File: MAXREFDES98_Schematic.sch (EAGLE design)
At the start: 34 parts, among them U1 MB110S-TP, U2 MB110S-TP, U3 MAX5969AETB+

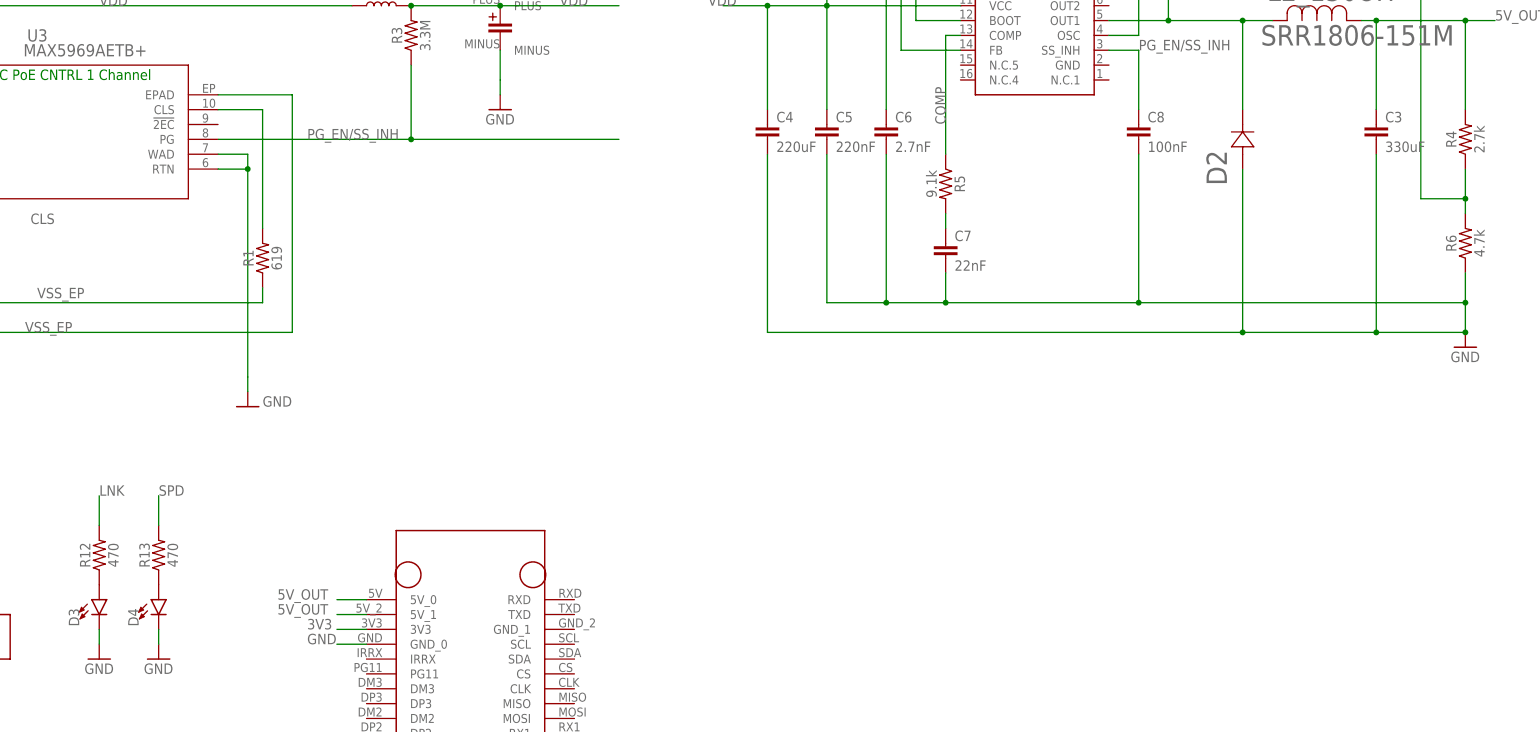
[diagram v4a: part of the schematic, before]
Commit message: Added new caps and leds
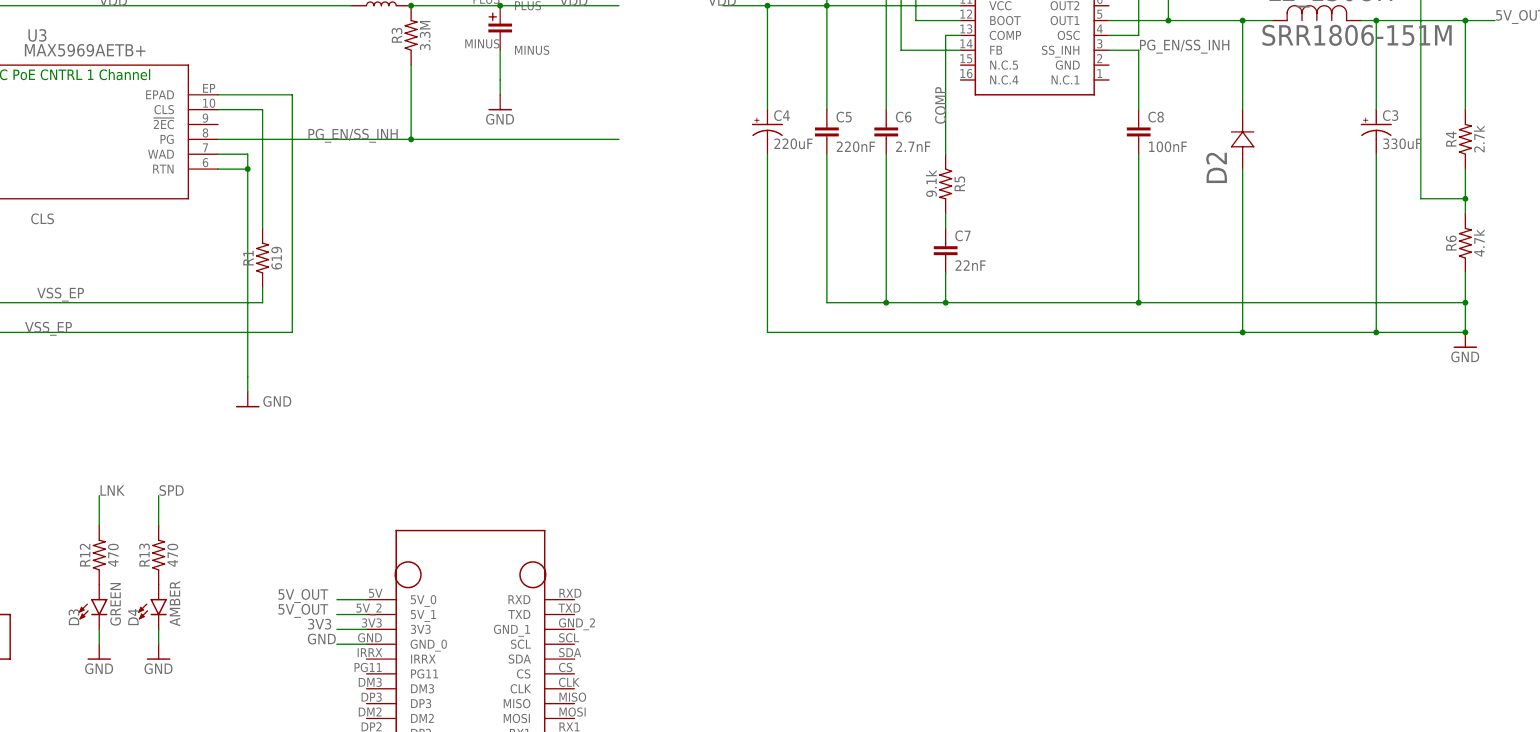
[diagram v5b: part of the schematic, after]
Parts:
- C3: value 330uF -> 337AXZ025M; device SparkFun-Capacitors:4.7UF0603 -> CameraBoard_Library:337AXZ025M
- C4: value 220uF -> EXV227M016A9HAA; device SparkFun-Capacitors:4.7UF0603 -> CameraBoard_Library:EXV227M016A9HAA
- D3: value (none) -> GREEN
- D4: value (none) -> AMBER
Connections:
- net 5V_OUT: now also C3.+; no longer C3.1
- net GND: now also C3.-, C4.-; no longer C3.2, C4.2
- net VDD: now also C4.+; no longer C4.1
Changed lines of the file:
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@@
 <part name="GND14" library="supply1" library_urn="urn:adsk.eagle:library:371" deviceset="GND" device=""/>
 <part name="U$1" library="Camera_Board_Parts_09_30_2020" deviceset="L4978D013TR" device="" package3d_urn="urn:adsk.eagle:package:24353853/1"/>
-<part name="C3" library="SparkFun-Capacitors" library_urn="urn:adsk.eagle:library:510" deviceset="4.7UF" device="0603" package3d_urn="urn:adsk.eagle:package:37414/1" value="330uF"/>
-<part name="C4" library="SparkFun-Capacitors" library_urn="urn:adsk.eagle:library:510" deviceset="4.7UF" device="0603" package3d_urn="urn:adsk.eagle:package:37414/1" value="220uF"/>
 <part name="C5" library="SparkFun-Capacitors" library_urn="urn:adsk.eagle:library:510" deviceset="4.7UF" device="0603" package3d_urn="urn:adsk.eagle:package:37414/1" value="220nF"/>
 <part name="C6" library="SparkFun-Capacitors" library_urn="urn:adsk.eagle:library:510" deviceset="4.7UF" device="0603" package3d_urn="urn:adsk.eagle:package:37414/1" value="2.7nF"/>
@@
 <part name="D2" library="Camera_Board_Parts_09_30_2020" deviceset="STPS3L60U" device="SMB_STM-M"/>
 <part name="GND2" library="supply1" library_urn="urn:adsk.eagle:library:371" deviceset="GND" device=""/>
-<part name="D3" library="SparkFun-LED" library_urn="urn:adsk.eagle:library:529" deviceset="LED" device="-FKIT-1206" package3d_urn="urn:adsk.eagle:package:39355/1"/>
-<part name="D4" library="SparkFun-LED" library_urn="urn:adsk.eagle:library:529" deviceset="LED" device="-FKIT-1206" package3d_urn="urn:adsk.eagle:package:39355/1"/>
+<part name="D3" library="SparkFun-LED" library_urn="urn:adsk.eagle:library:529" deviceset="LED" device="-FKIT-1206" package3d_urn="urn:adsk.eagle:package:39355/1" value="GREEN"/>
+<part name="D4" library="SparkFun-LED" library_urn="urn:adsk.eagle:library:529" deviceset="LED" device="-FKIT-1206" package3d_urn="urn:adsk.eagle:package:39355/1" value="AMBER"/>
 <part name="GND3" library="supply1" library_urn="urn:adsk.eagle:library:371" deviceset="GND" device=""/>
 <part name="GND4" library="supply1" library_urn="urn:adsk.eagle:library:371" deviceset="GND" device=""/>
@@
 <part name="L2_150UH" library="CameraBoard_Library" deviceset="SRR1806-151M" device=""/>
 <part name="U$2" library="CameraBoard_Library" deviceset="NANO_PI_CLEAN" device=""/>
+<part name="C4" library="CameraBoard_Library" deviceset="EXV227M016A9HAA" device=""/>
+<part name="C3" library="CameraBoard_Library" deviceset="337AXZ025M" device=""/>
 </parts>
 <sheets>
@@
 </instance>
 <instance part="U$1" gate="G$1" x="170.18" y="20.32" smashed="yes" rot="R180"/>
-<instance part="C3" gate="G$1" x="228.6" y="0" smashed="yes">
-<attribute name="NAME" x="230.124" y="2.921" size="1.778" layer="95" font="vector"/>
-<attribute name="VALUE" x="230.124" y="-2.159" size="1.778" layer="96" font="vector"/>
-</instance>
-<instance part="C4" gate="G$1" x="124.46" y="0" smashed="yes">
-<attribute name="NAME" x="125.984" y="2.921" size="1.778" layer="95" font="vector"/>
-<attribute name="VALUE" x="125.984" y="-2.159" size="1.778" layer="96" font="vector"/>
-</instance>
 <instance part="C5" gate="G$1" x="134.62" y="0" smashed="yes">
 <attribute name="NAME" x="136.144" y="2.921" size="1.778" layer="95" font="vector"/>
@@
 </instance>
 <instance part="U$2" gate="G$1" x="60.96" y="-121.92" smashed="yes"/>
+<instance part="C4" gate="G$1" x="124.46" y="2.54" smashed="yes">
+<attribute name="NAME" x="125.476" y="3.175" size="1.778" layer="95" font="vector"/>
+</instance>
+<instance part="C3" gate="G$1" x="228.6" y="2.54" smashed="yes">
+<attribute name="NAME" x="229.616" y="3.175" size="1.778" layer="95" font="vector"/>
+</instance>
 </instances>
 <busses>
@@
 <pinref part="U$1" gate="G$1" pin="VCC"/>
 <wire x1="157.48" y1="22.86" x2="134.62" y2="22.86" width="0.1524" layer="91"/>
-<pinref part="C4" gate="G$1" pin="1"/>
 <wire x1="134.62" y1="22.86" x2="124.46" y2="22.86" width="0.1524" layer="91"/>
 <wire x1="124.46" y1="22.86" x2="124.46" y2="5.08" width="0.1524" layer="91"/>
@@
 <junction x="124.46" y="22.86"/>
 <label x="114.3" y="22.86" size="1.778" layer="95"/>
+<pinref part="C4" gate="G$1" pin="+"/>
 </segment>
 <segment>
@@
 </segment>
 <segment>
-<pinref part="C3" gate="G$1" pin="1"/>
 <wire x1="228.6" y1="5.08" x2="228.6" y2="20.32" width="0.1524" layer="91"/>
 <wire x1="228.6" y1="20.32" x2="226.06" y2="20.32" width="0.1524" layer="91"/>
@@
 <label x="248.92" y="20.32" size="1.778" layer="95"/>
 <pinref part="L2_150UH" gate="A" pin="1"/>
+<pinref part="C3" gate="G$1" pin="+"/>
 </segment>
 <segment>
@@
 <wire x1="243.84" y1="-27.94" x2="243.84" y2="-33.02" width="0.1524" layer="91"/>
 <junction x="243.84" y="-27.94"/>
-<pinref part="C4" gate="G$1" pin="2"/>
 <wire x1="124.46" y1="-2.54" x2="124.46" y2="-33.02" width="0.1524" layer="91"/>
 <pinref part="D2" gate="A" pin="2"/>
@@
 <wire x1="205.74" y1="-33.02" x2="228.6" y2="-33.02" width="0.1524" layer="91"/>
 <junction x="205.74" y="-33.02"/>
-<pinref part="C3" gate="G$1" pin="2"/>
 <wire x1="228.6" y1="-33.02" x2="228.6" y2="-2.54" width="0.1524" layer="91"/>
 <wire x1="243.84" y1="-33.02" x2="228.6" y2="-33.02" width="0.1524" layer="91"/>
@@
 <pinref part="GND2" gate="1" pin="GND"/>
 <junction x="243.84" y="-33.02"/>
-</segment>
-<segment>
+<pinref part="C4" gate="G$1" pin="-"/>
+<pinref part="C3" gate="G$1" pin="-"/>
+</segment>
+<segment>

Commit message: Placement
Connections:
- new net VDD_L: C2.PLUS, C4.+, C5.1, L1.2, R3.2, R7.1, U$1.VCC
- net RD+: now also CONN.1; no longer CONN.5
- net RD-: now also CONN.2; no longer CONN.6
- net RECT1_IN_MINUS: now also CONN.6; no longer CONN.2
- net RECT1_IN_PLUS: now also CONN.5; no longer CONN.1
- net RECT2_IN_MINUS: now also CONN.7; no longer CONN.3
- net RECT2_IN_PLUS: now also CONN.8; no longer CONN.4
- net TD+: now also CONN.3; no longer CONN.7
- net TD-: now also CONN.4; no longer CONN.8
- net VDD: no longer C2.PLUS, C4.+, C5.1, L1.2, R3.2, R7.1, U$1.VCC
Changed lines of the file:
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@@
 <wire x1="-93.98" y1="22.86" x2="-93.98" y2="2.54" width="0.1524" layer="91"/>
 <wire x1="-93.98" y1="22.86" x2="-71.12" y2="22.86" width="0.1524" layer="91"/>
-<wire x1="-71.12" y1="22.86" x2="-71.12" y2="10.16" width="0.1524" layer="91"/>
+<wire x1="-71.12" y1="22.86" x2="-71.12" y2="2.54" width="0.1524" layer="91"/>
 <junction x="-93.98" y="22.86"/>
 <pinref part="D1" gate="G$1" pin="1"/>
-<wire x1="-71.12" y1="10.16" x2="-71.12" y2="2.54" width="0.1524" layer="91"/>
 <wire x1="-71.12" y1="22.86" x2="-55.88" y2="22.86" width="0.1524" layer="91"/>
 <junction x="-71.12" y="22.86"/>
-<wire x1="-55.88" y1="22.86" x2="-55.88" y2="5.08" width="0.1524" layer="91"/>
+<wire x1="-55.88" y1="22.86" x2="-55.88" y2="2.54" width="0.1524" layer="91"/>
 <pinref part="C1" gate="G$1" pin="1"/>
-<wire x1="-55.88" y1="5.08" x2="-55.88" y2="2.54" width="0.1524" layer="91"/>
 <wire x1="-55.88" y1="22.86" x2="-33.02" y2="22.86" width="0.1524" layer="91"/>
 <junction x="-55.88" y="22.86"/>
@@
 <wire x1="-25.4" y1="22.86" x2="-33.02" y2="22.86" width="0.1524" layer="91"/>
 <junction x="-33.02" y="22.86"/>
+<label x="10.16" y="22.86" size="1.778" layer="95"/>
+<pinref part="L1" gate="G$1" pin="1"/>
 <wire x1="-25.4" y1="22.86" x2="53.34" y2="22.86" width="0.1524" layer="91"/>
 <junction x="-25.4" y="22.86"/>
-<pinref part="L1" gate="G$1" pin="1"/>
-<label x="10.16" y="22.86" size="1.778" layer="95"/>
-</segment>
-<segment>
-<pinref part="U$1" gate="G$1" pin="VCC"/>
-<wire x1="157.48" y1="22.86" x2="134.62" y2="22.86" width="0.1524" layer="91"/>
-<wire x1="134.62" y1="22.86" x2="124.46" y2="22.86" width="0.1524" layer="91"/>
-<wire x1="124.46" y1="22.86" x2="124.46" y2="5.08" width="0.1524" layer="91"/>
-<pinref part="C5" gate="G$1" pin="1"/>
-<wire x1="134.62" y1="5.08" x2="134.62" y2="22.86" width="0.1524" layer="91"/>
-<junction x="134.62" y="22.86"/>
-<pinref part="R7" gate="G$1" pin="1"/>
-<wire x1="134.62" y1="35.56" x2="134.62" y2="22.86" width="0.1524" layer="91"/>
-<wire x1="124.46" y1="22.86" x2="116.84" y2="22.86" width="0.1524" layer="91"/>
-<junction x="124.46" y="22.86"/>
-<label x="114.3" y="22.86" size="1.778" layer="95"/>
-<pinref part="C4" gate="G$1" pin="+"/>
-</segment>
-<segment>
-<pinref part="C2" gate="G$1" pin="PLUS"/>
-<pinref part="R3" gate="G$1" pin="2"/>
-<wire x1="63.5" y1="22.86" x2="78.74" y2="22.86" width="0.1524" layer="91"/>
-<pinref part="L1" gate="G$1" pin="2"/>
-<junction x="63.5" y="22.86"/>
-<label x="88.9" y="22.86" size="1.778" layer="95"/>
-<wire x1="78.74" y1="22.86" x2="99.06" y2="22.86" width="0.1524" layer="91"/>
-<junction x="78.74" y="22.86"/>
 </segment>
 </net>
@@
 <net name="RD+" class="0">
 <segment>
-<wire x1="-15.24" y1="-78.74" x2="-15.24" y2="-73.66" width="0.1524" layer="91"/>
-<pinref part="CONN" gate="G$1" pin="5"/>
-<label x="-15.24" y="-73.66" size="1.778" layer="95" rot="R90"/>
-</segment>
-<segment>
 <wire x1="55.88" y1="-106.68" x2="50.8" y2="-106.68" width="0.1524" layer="91"/>
 <label x="50.8" y="-104.14" size="1.778" layer="95" rot="R180"/>
 <pinref part="U$2" gate="G$1" pin="RD+"/>
 </segment>
+<segment>
+<pinref part="CONN" gate="G$1" pin="1"/>
+<wire x1="-25.4" y1="-78.74" x2="-25.4" y2="-71.12" width="0.1524" layer="91"/>
+<label x="-25.4" y="-71.12" size="1.778" layer="95" rot="R90"/>
+</segment>
 </net>
 <net name="RECT1_IN_MINUS" class="0">
-<segment>
-<pinref part="CONN" gate="G$1" pin="2"/>
-<wire x1="-22.86" y1="-78.74" x2="-22.86" y2="-73.66" width="0.1524" layer="91"/>
-<label x="-22.86" y="-73.66" size="1.778" layer="95" rot="R90"/>
-</segment>
 <segment>
 <pinref part="U1" gate="G$1" pin="~1"/>
@@
 <label x="-116.84" y="-20.32" size="1.778" layer="95" rot="R90"/>
 </segment>
+<segment>
+<wire x1="-12.7" y1="-78.74" x2="-12.7" y2="-71.12" width="0.1524" layer="91"/>
+<pinref part="CONN" gate="G$1" pin="6"/>
+<label x="-12.7" y="-71.12" size="1.778" layer="95" rot="R90"/>
+</segment>
 </net>
 <net name="RECT1_IN_PLUS" class="0">
-<segment>
-<pinref part="CONN" gate="G$1" pin="1"/>
-<wire x1="-25.4" y1="-78.74" x2="-25.4" y2="-73.66" width="0.1524" layer="91"/>
-<label x="-25.4" y="-73.66" size="1.778" layer="95" rot="R90"/>
-</segment>
 <segment>
 <pinref part="U1" gate="G$1" pin="~2"/>
@@
 <label x="-106.68" y="-20.32" size="1.778" layer="95" rot="R90"/>
 </segment>
+<segment>
+<wire x1="-15.24" y1="-78.74" x2="-15.24" y2="-71.12" width="0.1524" layer="91"/>
+<pinref part="CONN" gate="G$1" pin="5"/>
+<label x="-15.24" y="-71.12" size="1.778" layer="95" rot="R90"/>
+</segment>
 </net>
 <net name="RECT2_IN_MINUS" class="0">
-<segment>
-<pinref part="CONN" gate="G$1" pin="3"/>
-<wire x1="-20.32" y1="-78.74" x2="-20.32" y2="-73.66" width="0.1524" layer="91"/>
-<label x="-20.32" y="-73.66" size="1.778" layer="95" rot="R90"/>
-</segment>
 <segment>
 <pinref part="U2" gate="G$1" pin="~1"/>
@@
 <label x="-99.06" y="-20.32" size="1.778" layer="95" rot="R90"/>
 </segment>
+<segment>
+<wire x1="-10.16" y1="-78.74" x2="-10.16" y2="-71.12" width="0.1524" layer="91"/>
+<pinref part="CONN" gate="G$1" pin="7"/>
+<label x="-10.16" y="-71.12" size="1.778" layer="95" rot="R90"/>
+</segment>
 </net>
 <net name="RECT2_IN_PLUS" class="0">
-<segment>
-<pinref part="CONN" gate="G$1" pin="4"/>
-<wire x1="-17.78" y1="-78.74" x2="-17.78" y2="-73.66" width="0.1524" layer="91"/>
-<label x="-17.78" y="-73.66" size="1.778" layer="95" rot="R90"/>
-</segment>
 <segment>
 <pinref part="U2" gate="G$1" pin="~2"/>
@@
 <label x="-91.44" y="-20.32" size="1.778" layer="95" rot="R90"/>
 </segment>
+<segment>
+<wire x1="-7.62" y1="-78.74" x2="-7.62" y2="-71.12" width="0.1524" layer="91"/>
+<pinref part="CONN" gate="G$1" pin="8"/>
+<label x="-7.62" y="-71.12" size="1.778" layer="95" rot="R90"/>
+</segment>
 </net>
 <net name="RD-" class="0">
-<segment>
-<pinref part="CONN" gate="G$1" pin="6"/>
-<wire x1="-12.7" y1="-78.74" x2="-12.7" y2="-73.66" width="0.1524" layer="91"/>
-<label x="-12.7" y="-73.66" size="1.778" layer="95" rot="R90"/>
-</segment>
 <segment>
 <wire x1="55.88" y1="-104.14" x2="50.8" y2="-104.14" width="0.1524" layer="91"/>
@@
 <pinref part="U$2" gate="G$1" pin="RD-"/>
 </segment>
+<segment>
+<wire x1="-22.86" y1="-78.74" x2="-22.86" y2="-71.12" width="0.1524" layer="91"/>
+<pinref part="CONN" gate="G$1" pin="2"/>
+<label x="-22.86" y="-71.12" size="1.778" layer="95" rot="R90"/>
+</segment>
 </net>
 <net name="TD+" class="0">
-<segment>
-<pinref part="CONN" gate="G$1" pin="7"/>
-<wire x1="-10.16" y1="-78.74" x2="-10.16" y2="-73.66" width="0.1524" layer="91"/>
-<label x="-10.16" y="-73.66" size="1.778" layer="95" rot="R90"/>
-</segment>
 <segment>
 <wire x1="55.88" y1="-111.76" x2="50.8" y2="-111.76" width="0.1524" layer="91"/>
@@
 <pinref part="U$2" gate="G$1" pin="TD+"/>
 </segment>
+<segment>
+<wire x1="-20.32" y1="-78.74" x2="-20.32" y2="-71.12" width="0.1524" layer="91"/>
+<pinref part="CONN" gate="G$1" pin="3"/>
+<label x="-20.32" y="-71.12" size="1.778" layer="95" rot="R90"/>
+</segment>
 </net>
 <net name="TD-" class="0">
-<segment>
-<pinref part="CONN" gate="G$1" pin="8"/>
-<wire x1="-7.62" y1="-78.74" x2="-7.62" y2="-73.66" width="0.1524" layer="91"/>
-<label x="-7.62" y="-73.66" size="1.778" layer="95" rot="R90"/>
-</segment>
 <segment>
 <wire x1="55.88" y1="-109.22" x2="50.8" y2="-109.22" width="0.1524" layer="91"/>
 <label x="50.8" y="-106.68" size="1.778" layer="95" rot="R180"/>
 <pinref part="U$2" gate="G$1" pin="TD-"/>
+</segment>
+<segment>
+<wire x1="-17.78" y1="-78.74" x2="-17.78" y2="-71.12" width="0.1524" layer="91"/>
+<pinref part="CONN" gate="G$1" pin="4"/>
+<label x="-17.78" y="-71.12" size="1.778" layer="95" rot="R90"/>
 </segment>
 </net>
@@
 </segment>
 </net>
+<net name="VDD_L" class="0">
+<segment>
+<pinref part="C2" gate="G$1" pin="PLUS"/>
+<label x="88.9" y="22.86" size="1.778" layer="95"/>
+<wire x1="78.74" y1="22.86" x2="99.06" y2="22.86" width="0.1524" layer="91"/>
+<pinref part="R3" gate="G$1" pin="2"/>
+<pinref part="L1" gate="G$1" pin="2"/>
+<wire x1="63.5" y1="22.86" x2="78.74" y2="22.86" width="0.1524" layer="91"/>
+<junction x="63.5" y="22.86"/>
+<junction x="78.74" y="22.86"/>
+</segment>
+<segment>
+<pinref part="U$1" gate="G$1" pin="VCC"/>
+<wire x1="157.48" y1="22.86" x2="134.62" y2="22.86" width="0.1524" layer="91"/>
+<wire x1="134.62" y1="22.86" x2="124.46" y2="22.86" width="0.1524" layer="91"/>
+<wire x1="124.46" y1="22.86" x2="124.46" y2="5.08" width="0.1524" layer="91"/>
+<pinref part="C5" gate="G$1" pin="1"/>
+<wire x1="134.62" y1="5.08" x2="134.62" y2="22.86" width="0.1524" layer="91"/>
+<junction x="134.62" y="22.86"/>
+<pinref part="R7" gate="G$1" pin="1"/>
+<wire x1="134.62" y1="35.56" x2="134.62" y2="22.86" width="0.1524" layer="91"/>
+<wire x1="124.46" y1="22.86" x2="116.84" y2="22.86" width="0.1524" layer="91"/>
+<junction x="124.46" y="22.86"/>
+<label x="114.3" y="22.86" size="1.778" layer="95"/>
+<pinref part="C4" gate="G$1" pin="+"/>
+</segment>
+</net>

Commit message: re-route ethernet. clean up a few things
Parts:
- C1: device SparkFun-Capacitors:1.0UF-0805-25V-(+80/-20%) -> SparkFun-Capacitors:0.1UF-0603-25V-5%
- CONN: value TERM_BLOCK_PLUG_8POS_STR_2.5MM -> PXC-8-RA-1778683; device Camera_Board_Parts_09_30_2020:TERM_BLOCK_PLUG_8POS_STR_2.5MM -> Phoenix Contact PTSM 8 pin:PXC-8-RA-1778683
- R4: device SparkFun-Resistors:0.22OHM-0805-1/4W-1% -> SparkFun-Resistors:20OHM-0603-1/10W-1%
- R5, R6: device SparkFun-Resistors:0.22OHM-0805-1/4W-1% -> SparkFun-Resistors:470OHM-0603-1/10W-1%
- R7: device SparkFun-Resistors:0.22OHM-0805-1/4W-1% -> SparkFun-Resistors:22KOHM-0603-1/10W-1%
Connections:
- removed net RD+: CONN.1, U$2.RD+
- removed net RD-: CONN.2, U$2.RD-
- removed net TD+: CONN.3, U$2.TD+
- removed net TD-: CONN.4, U$2.TD-
- new net RD_N: CONN.1, U$2.RD-
- new net RD_P: CONN.2, U$2.RD+
- new net TD_N: CONN.3, U$2.TD-
- new net TD_P: CONN.4, U$2.TD+
- net IND_IN: now also U$1.OUT2
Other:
- moved on the sheet: C1, C3, C4, C5, C6, C7, C8, C9, CONN, D1, D2, D3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
